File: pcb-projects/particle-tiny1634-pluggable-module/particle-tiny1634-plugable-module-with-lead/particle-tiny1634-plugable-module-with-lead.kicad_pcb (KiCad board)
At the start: 2 copper layers, 41.3 x 48.3 mm, 33 parts, among them IC1 ATTINY1634-SU, P1 INTERFACE, P2 MCU_TEST

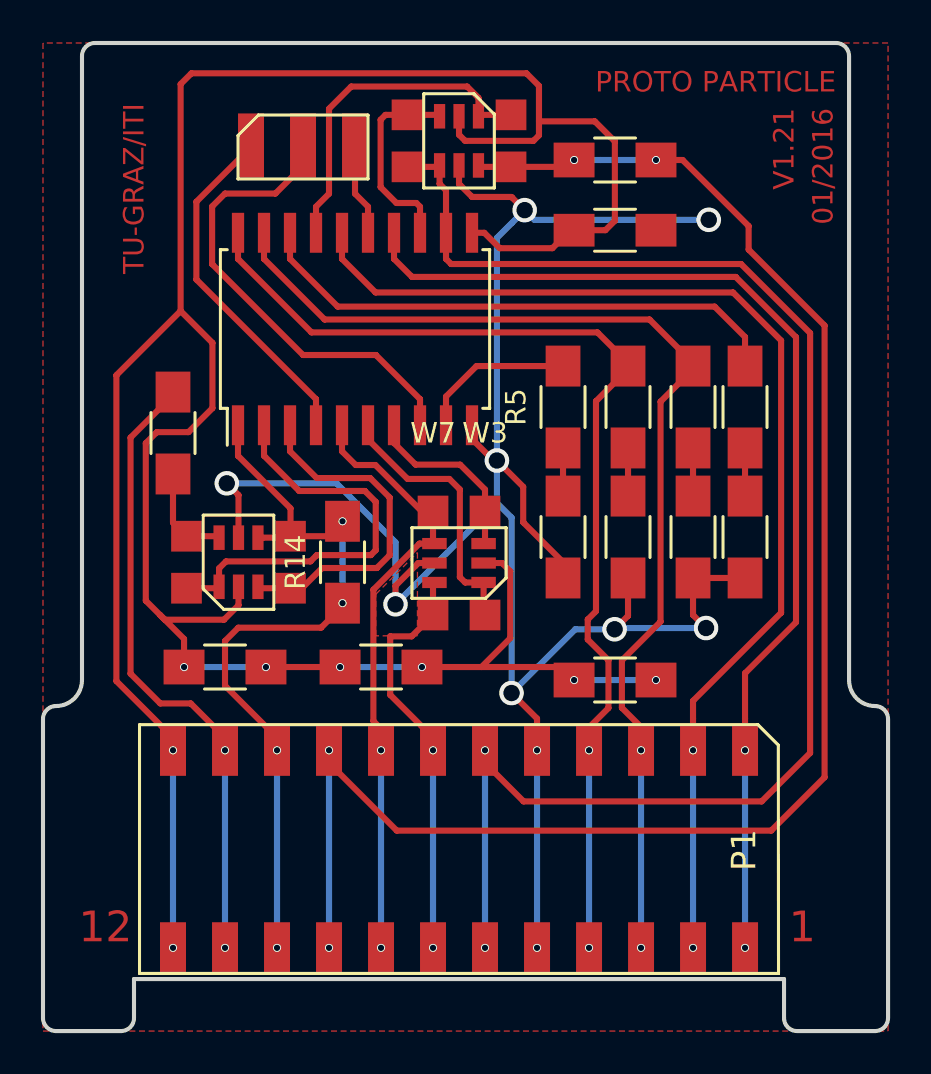
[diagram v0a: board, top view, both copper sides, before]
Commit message: change shape, updated euro pcb
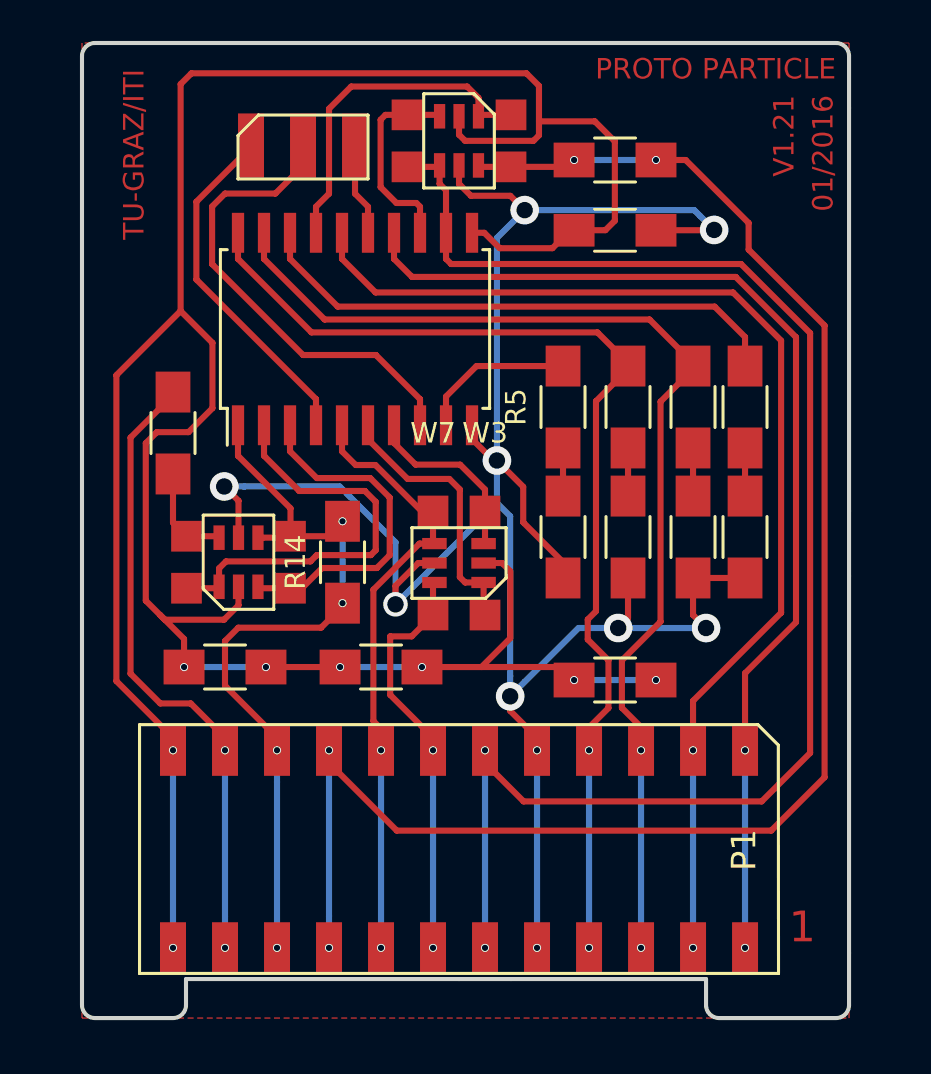
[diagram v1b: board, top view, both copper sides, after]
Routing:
- net GND: track 105.1 -> 108.4 mm
- net /RX-SOUTH: track 29.8 -> 29.1 mm
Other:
- board size 41.3 x 48.3 mm -> 37.5 x 47.6 mm
- net class Default: via_dia 1.2 -> 1.4
- board text removed: "12"

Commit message: grid board illustration is now in grey
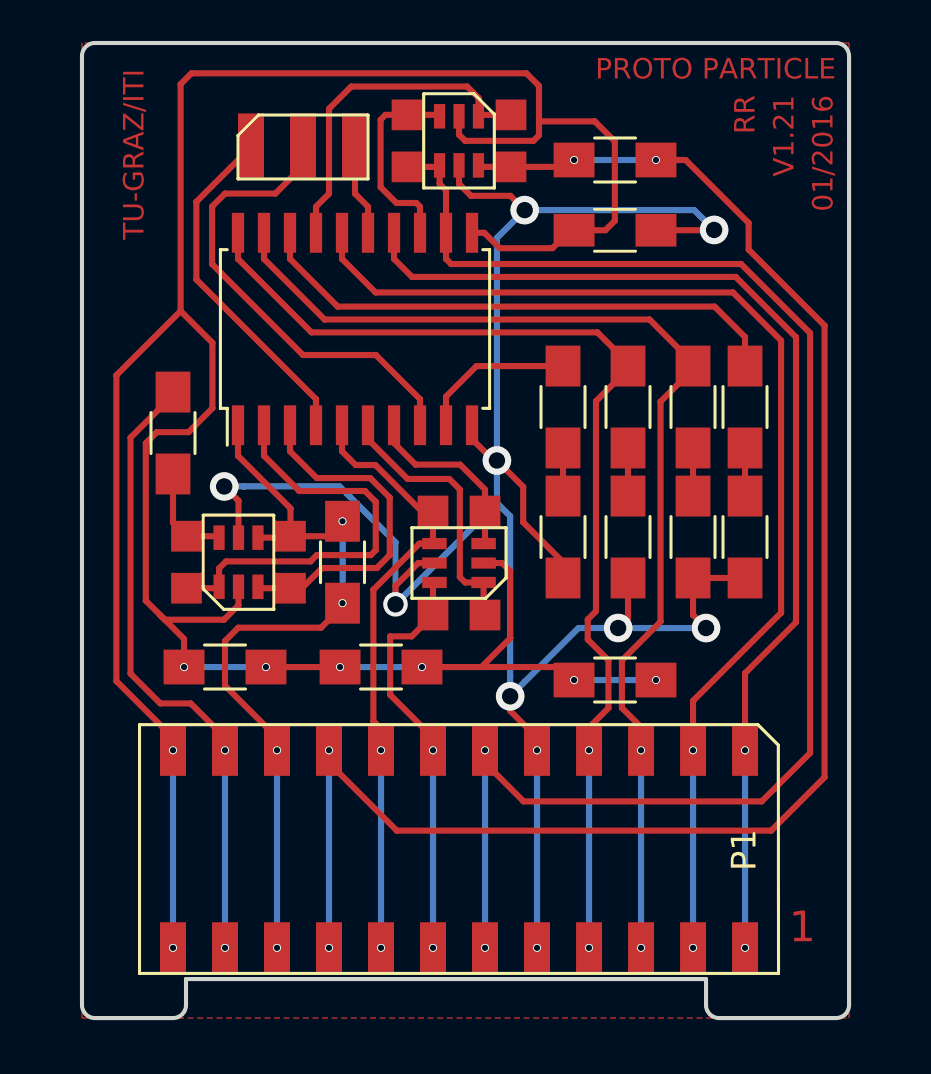
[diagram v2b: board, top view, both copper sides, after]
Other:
- board text added: "RR"
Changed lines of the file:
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@@
     (links 79)
     (no_connects 0)
-    (area 126.461787 79.7 181.99 143.035001)
+    (area 128.804999 83.719999 166.470001 131.545001)
     (thickness 1.6)
-    (drawings 38)
+    (drawings 39)
     (tracks 362)
     (zones 0)
@@
     (pad_to_mask_clearance 0.2)
     (aux_axis_origin 0 0)
-    (visible_elements FFFFFF9F)
+    (visible_elements FFFFFFBF)
     (pcbplotparams
       (layerselection 0x00030_80000001)
@@
     (tags "resistor 1206")
     (attr smd)
-    (fp_text reference R5 (at 0 -2.3 90) (layer F.SilkS)
+    (fp_text reference R5 (at 0 -2.3 90) (layer F.SilkS) hide
       (effects (font (size 1 1) (thickness 0.15)))
     )
@@
     (descr "Mesurement Point, Square, SMD Pad,  1.5mm x 1.5mm,")
     (tags "Mesurement Point, Square, SMD Pad, 1.5mm x 1.5mm,")
-    (fp_text reference W3 (at 0 -3.81) (layer F.SilkS)
+    (fp_text reference W3 (at 0 -3.81) (layer F.SilkS) hide
       (effects (font (size 1 1) (thickness 0.15)))
     )
@@
     (descr "Mesurement Point, Square, SMD Pad,  1.5mm x 1.5mm,")
     (tags "Mesurement Point, Square, SMD Pad, 1.5mm x 1.5mm,")
-    (fp_text reference W7 (at 0 -3.81) (layer F.SilkS)
+    (fp_text reference W7 (at 0 -3.81) (layer F.SilkS) hide
       (effects (font (size 1 1) (thickness 0.15)))
     )
@@
     (tags "resistor 1206")
     (attr smd)
-    (fp_text reference R14 (at 0 -2.3 90) (layer F.SilkS)
+    (fp_text reference R14 (at 0 -2.3 90) (layer F.SilkS) hide
       (effects (font (size 1 1) (thickness 0.15)))
     )
@@
     )
   )
+  (gr_text RR (at 161.29 86.36 90) (layer F.Cu)
+    (effects (font (size 1 1) (thickness 0.2)) (justify right))
+  )
   (gr_line (start 149.86 129.54) (end 159.385 129.54) (layer Edge.Cuts) (width 0.2))

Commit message: cleanup folders; minimal pcb changes
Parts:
- renumbered Q-CHAIN1 to Q-EAST1
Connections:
- net /PWR/TX-CHAIN renamed /SW_PWR_TX-EAST
- net /PWR/TX-NORTH renamed /SW_PWR_TX-NORTH
- net /PWR/TX-SOUTH renamed /SW_PWR_TX-SOUTH
- net /RX-CHAIN renamed /RX-EAST
- net /SW_PWR/RX-CHAIN renamed /SW_PWR_RX-EAST
- net /SW_PWR/RX-NORTH renamed /SW_PWR_RX-NORTH
- net /SW_PWR/RX-SOUTH renamed /SW_PWR_RX-SOUTH
- net /TX-CHAIN renamed /TX-EAST
